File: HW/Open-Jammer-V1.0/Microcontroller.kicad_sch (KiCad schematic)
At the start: 1 part, among them U5 ESP32-S3-WROOM-1-N16R2

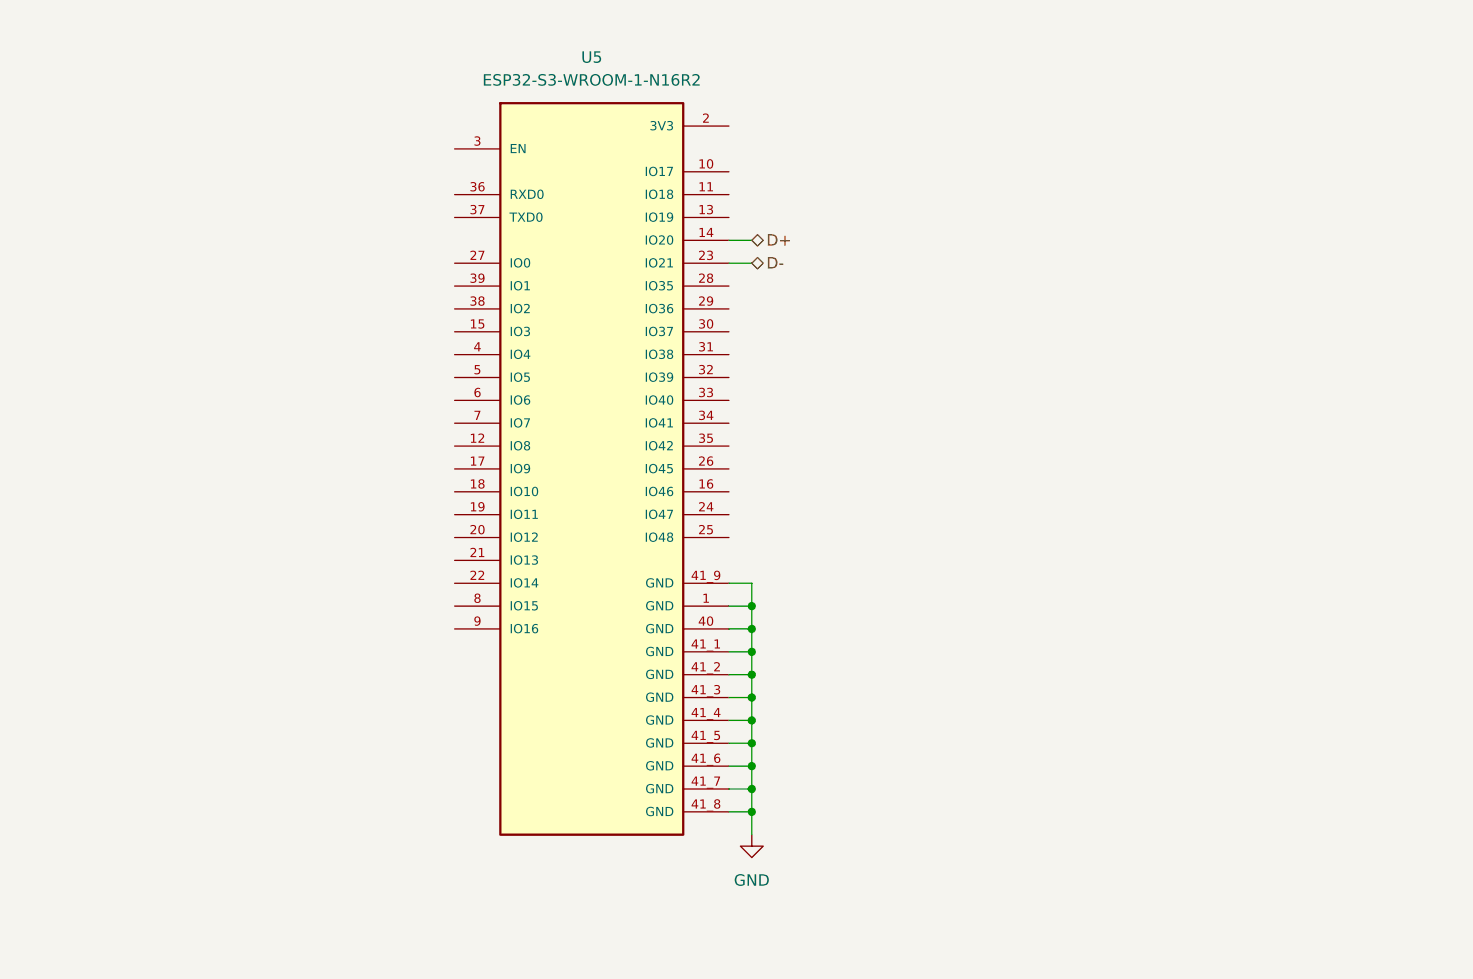
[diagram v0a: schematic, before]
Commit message: Added reset and boot buttons. Added oled screen. Added ESP32 VCC capacitors
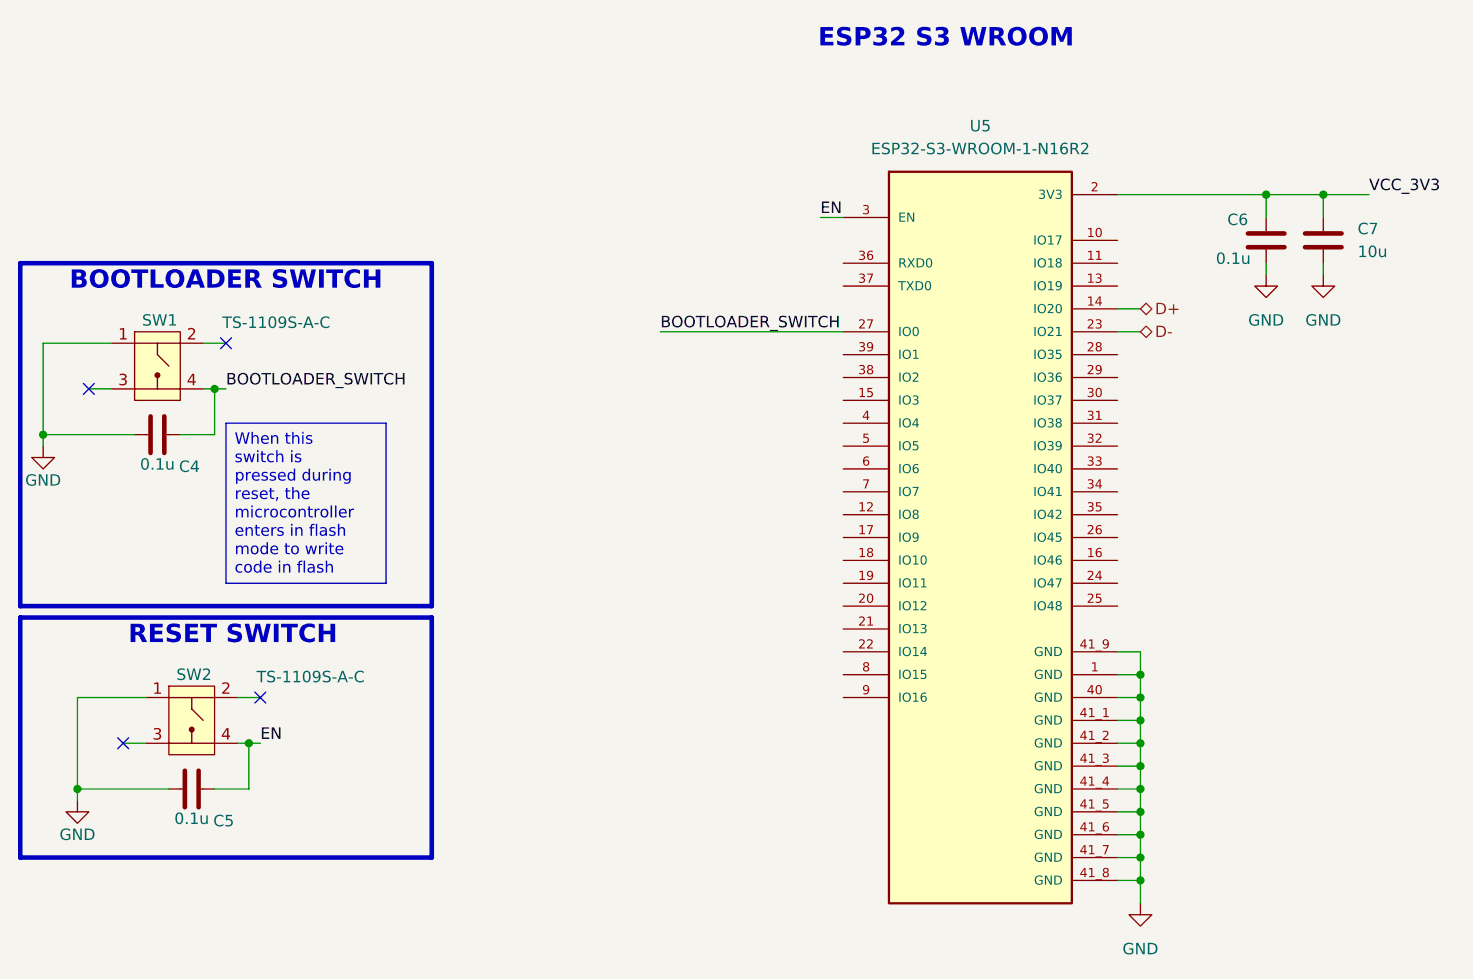
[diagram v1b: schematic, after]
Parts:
- added C4, C5, C6: 0.1u, symbol Open-Jammer:CAP_0.1u_10%_X7R_16V_0603
- added C7: 10u, symbol Open-Jammer:CAP_10u_20%_X5R_25V_0603
- added SW1, SW2: TS-1109S-A-C, Open-Jammer:TACTILE_SWITCH_SMD, symbol Open-Jammer:TACTILE_SWITCH_SPST_SMD
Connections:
- net GND: now also C4.1, C5.1, C6.1, C7.1, SW1.1 (P1), SW2.1 (P1)
- net VCC_3V3: now reaches U5.2 (3V3)
- net VCC_3V3: now also C6.2, C7.2
- net BOOTLOADER_SWITCH: now reaches U5.27 (IO0)
- net BOOTLOADER_SWITCH: now also C4.2, SW1.4
- net EN: now reaches U5.3 (EN)
- net EN: now also C5.2, SW2.4
- no-connect marks 0 -> 4
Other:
- note added: "BOOTLOADER SWITCH"
- note added: "ESP32 S3 WROOM"
- note added: "RESET SWITCH"
- title: (none) -> Oper Jammer V1R0
- moved on the sheet: U5
